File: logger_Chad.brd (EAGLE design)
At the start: 99 x 44.1 mm, 65 parts, among them IC1 LTC4412, J1 POWER_JACKPTH, Q1 FDN360P, Q2 FDN360P, Q3 2N7002PW, Q4 2N7002PW, U1 FT232RL

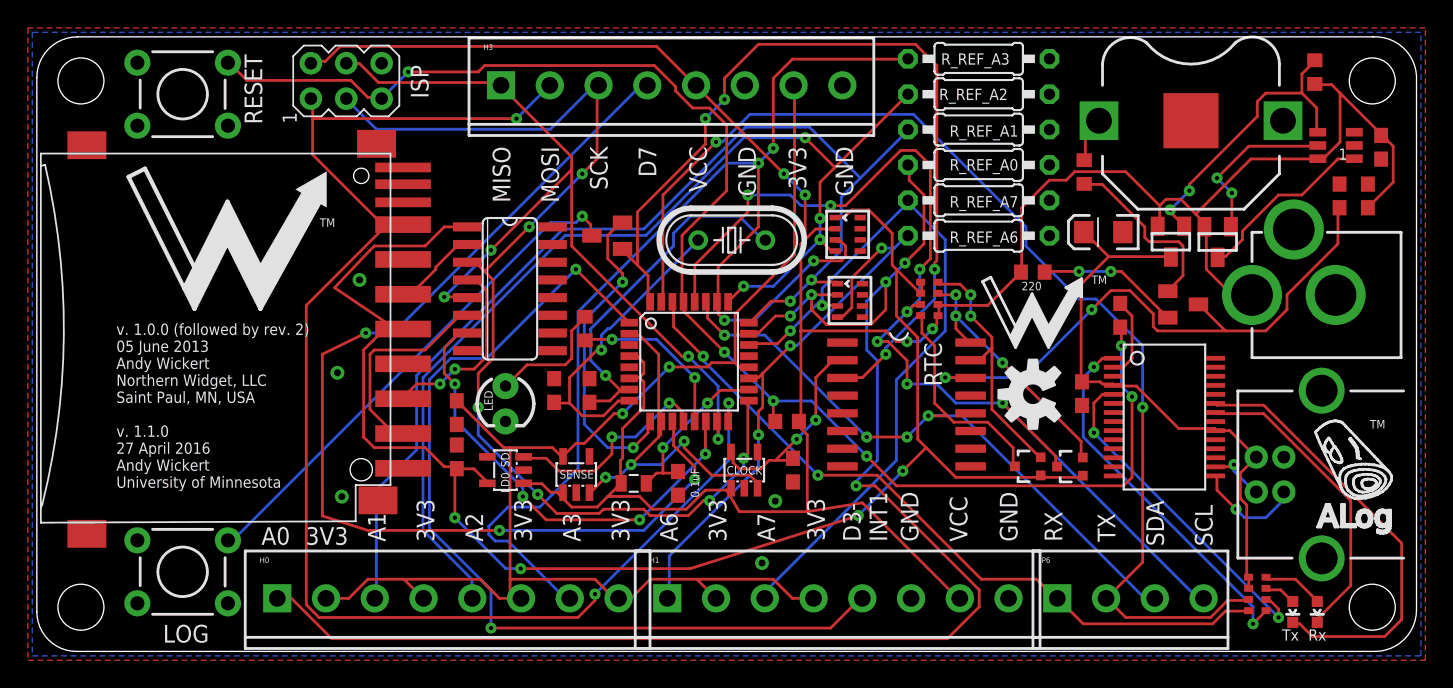
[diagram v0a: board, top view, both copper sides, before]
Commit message: Routed board, ground fills and minimized timing device distances
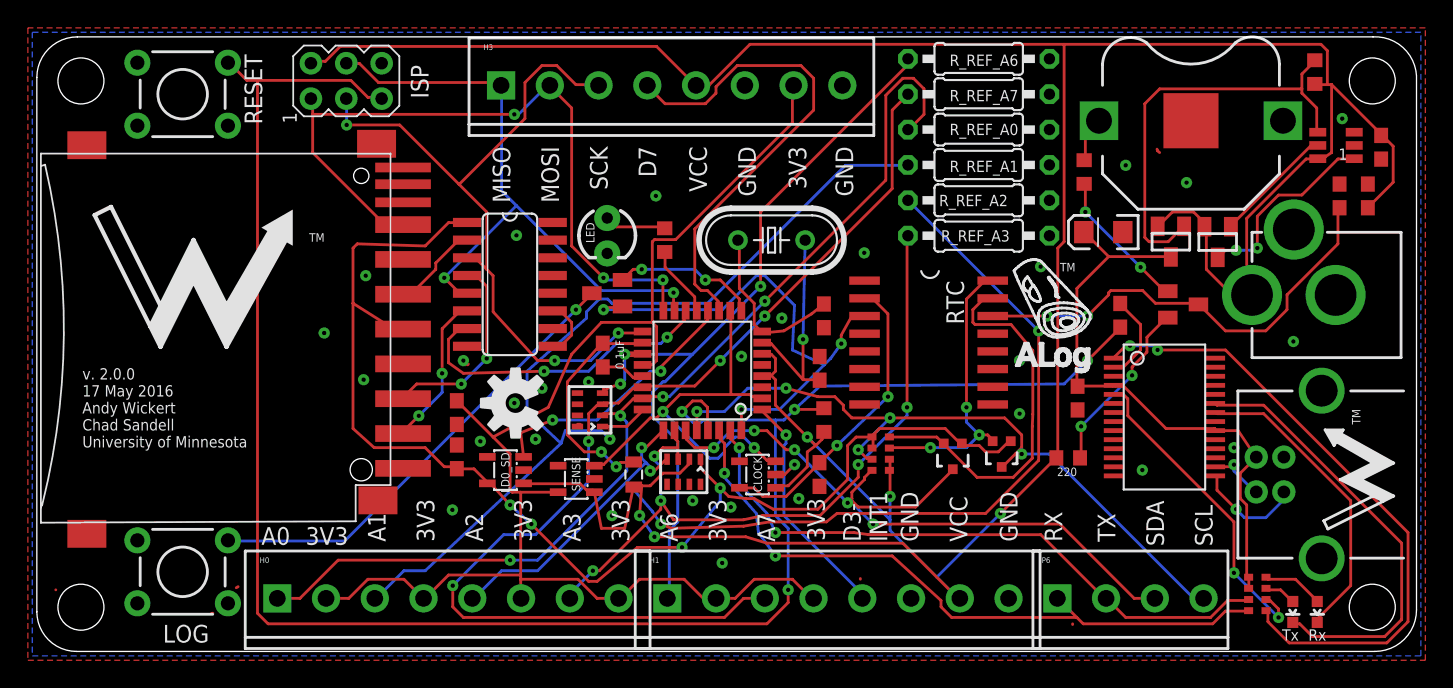
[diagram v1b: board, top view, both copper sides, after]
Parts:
- moved LOGO1 37.2 mm to (34.4, 17.8)
- moved U$3 26.2 mm to (94.5, 12.3), turned to 90 degrees
- moved U$2 24.5 mm to (73.0, 25.3)
- moved C14 20.7 mm to (46.5, 12.9), turned to 180 degrees
- moved C15 20.2 mm to (39.7, 17.3), turned to 90 degrees
- moved CX1 20.1 mm to (56.5, 24.1), turned to 90 degrees
- moved CX0 16.6 mm to (56.2, 20.3)
- moved LED 14.1 mm to (41.0, 29.8)
- moved RCKL1 13.6 mm to (74.1, 13.9)
- moved R_REF_A3 12.7 mm to (67.6, 29.8)
- moved R_REF_A6 12.7 mm to (67.6, 42.5)
- moved RN2 11.6 mm to (60.6, 14.2)
- moved ADECOUP 10.7 mm to (40.6, 21.3)
- moved R_LED 8.54 mm to (45.1, 29.5)
- moved R_REF_A2 7.62 mm to (67.6, 32.4)
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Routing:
- net VCC: track 194.6 -> 245.6 mm, vias 4 -> 5
- net DO: track 102.7 -> 52.5 mm
- net D3-INT1: track 66.4 -> 16.7 mm, vias 2 -> 1
- net D7-CS-EXT: track 75.9 -> 35.5 mm, vias 3 -> 0
- net RESET: track 104.9 -> 143.5 mm, vias 6 -> 4
- net TX-O: track 82.8 -> 45.5 mm
- net A0: track 108.7 -> 73.7 mm, vias 5 -> 4
- net A3: track 86.9 -> 52.5 mm, vias 4 -> 5
- net INT0: track 63.6 -> 36.6 mm, vias 4 -> 3
- net CLK: track 79.1 -> 52.5 mm, vias 6 -> 3
- net SCL: track 78.4 -> 52.0 mm, vias 7 -> 5
- net VDD: track 116.1 -> 90.3 mm
- net A7: track 53.0 -> 78.3 mm, vias 2 -> 4
- net N$27: track 26.8 -> 45.7 mm
- net A6: track 42.1 -> 57.9 mm
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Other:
- board text added: "v. 2.0.0 17 May 2016 Andy Wickert Chad Sandell University of Minnesota"
- board text removed: "v. 1.0.0 (followed by rev. 2) 05 June 2013 Andy Wickert Northern Widget, LLC Saint Paul, MN, USA v. 1.1.0 27 April 2016 Andy Wickert University of Minnesota"
